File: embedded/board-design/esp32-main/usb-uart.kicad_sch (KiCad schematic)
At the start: 16 parts, among them J2 0473460001, U3 FT231XS

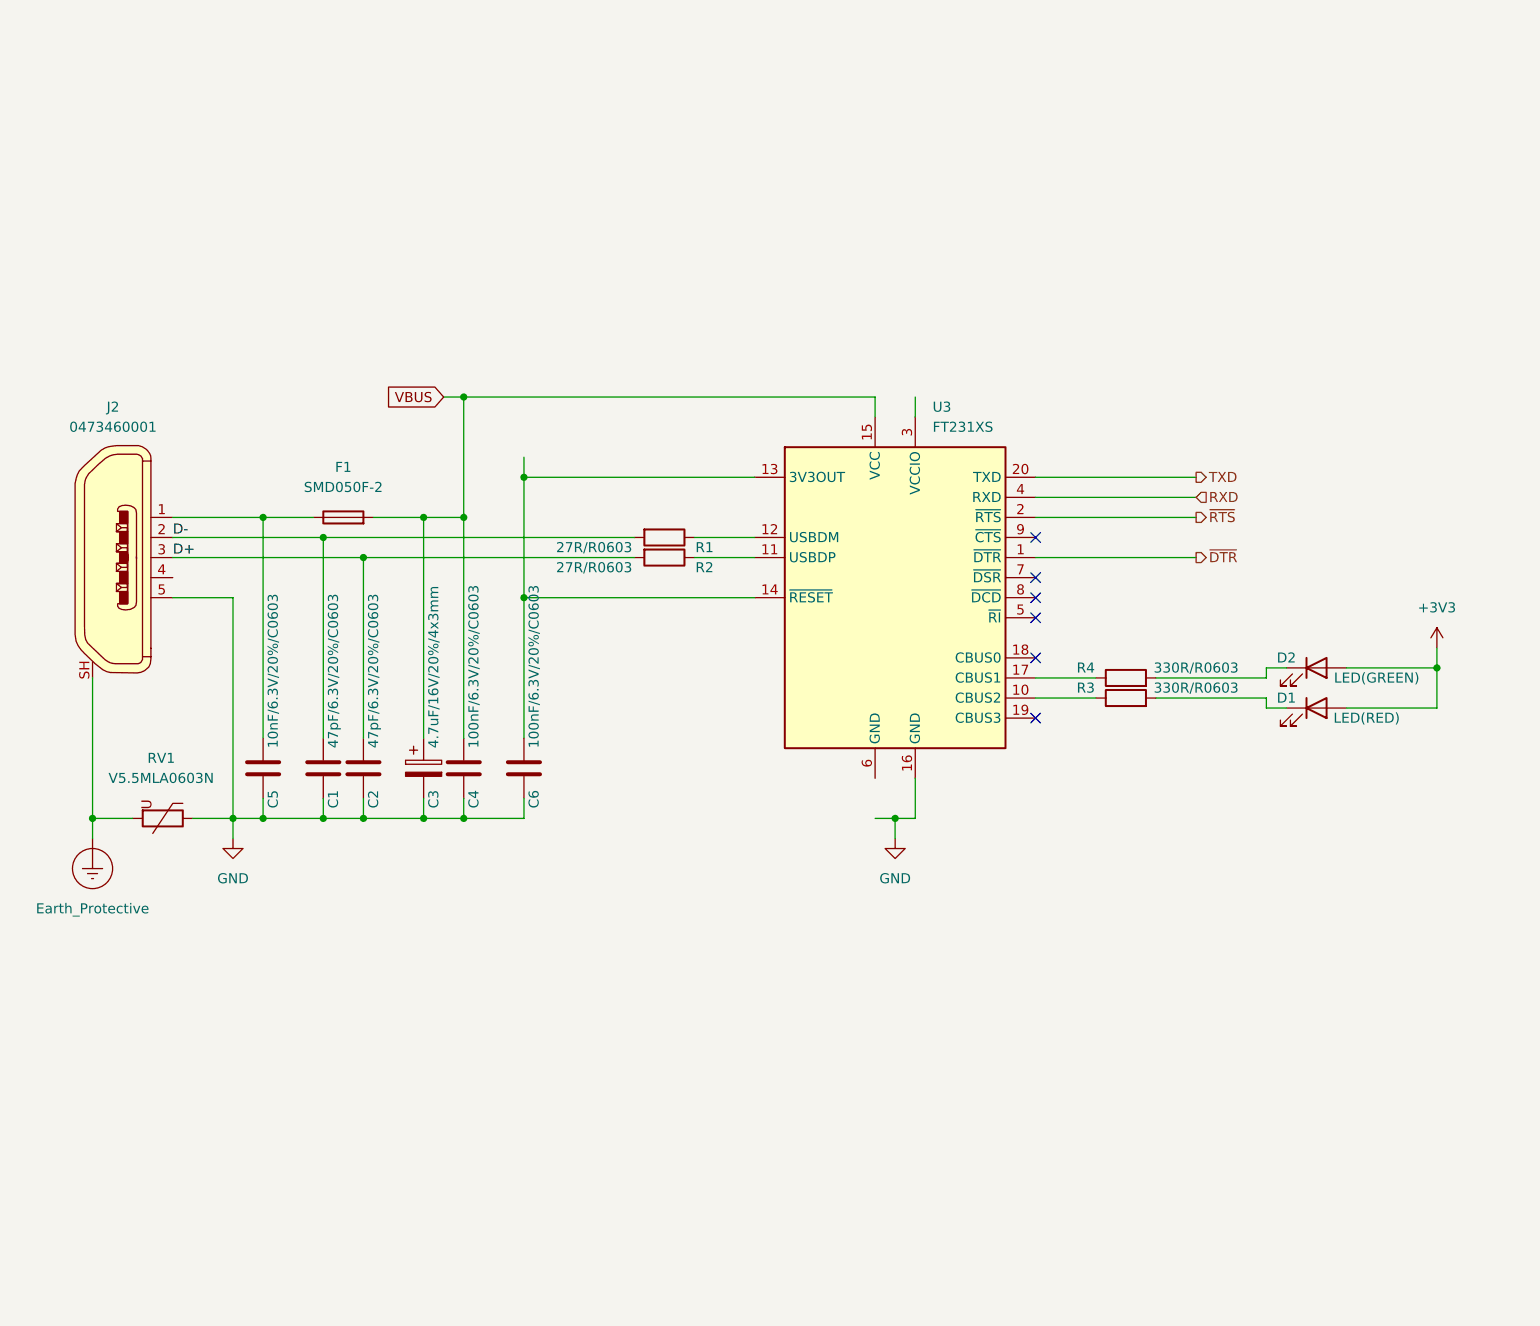
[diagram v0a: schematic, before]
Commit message: [bike-embedded-app]
Finished first schematic draft.

Signed-off-by: Nicolae-Andrei Vasile <vasilenicolaeandrei@gmail.com>
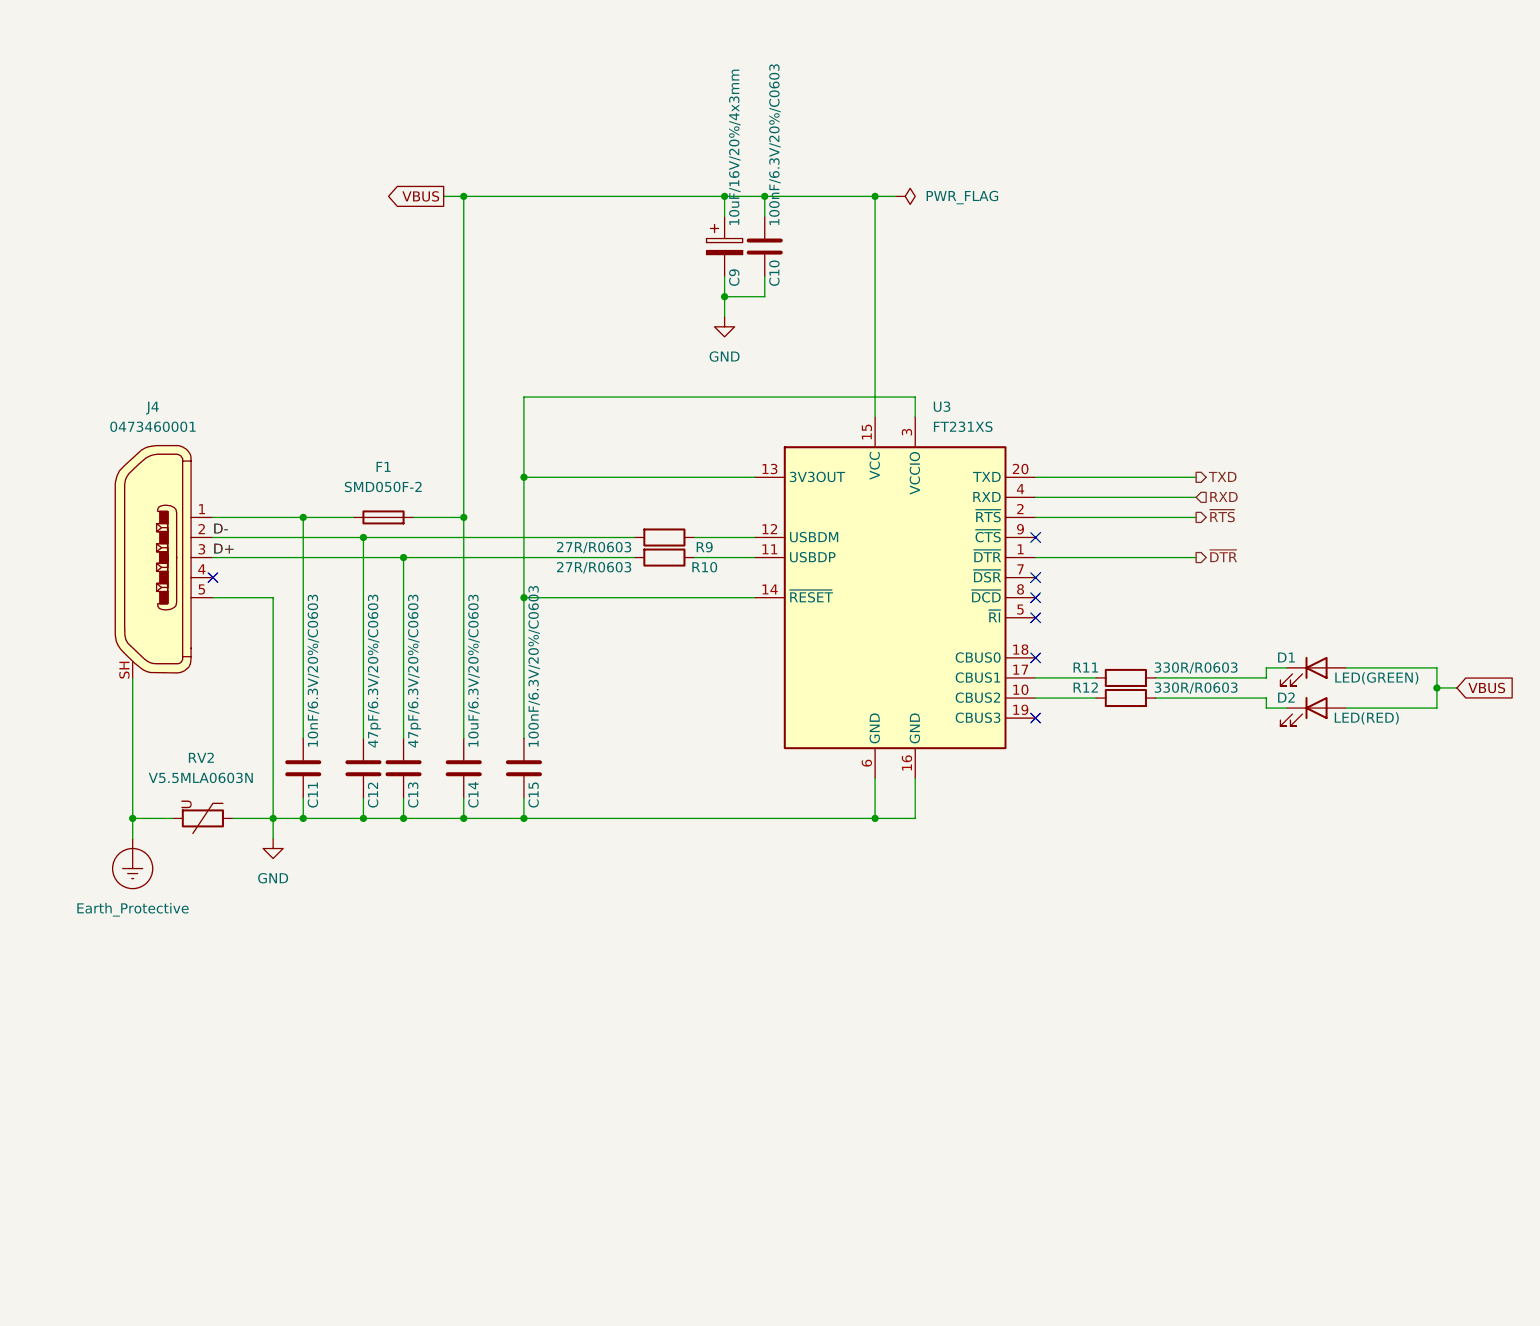
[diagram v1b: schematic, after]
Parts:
- added C14: 10uF/6.3V/20%/C0603, Capacitor_SMD:C_0603_1608Metric_Pad1.08x0.95mm_HandSolder, symbol Device:C
- C9: renamed from C3; value 4.7uF/16V/20%/4x3mm -> 10uF/16V/20%/4x3mm
- RV2: renamed from RV1; footprint (none) -> Resistor_SMD:R_0603_1608Metric_Pad0.98x0.95mm_HandSolder
- renumbered C4 to C10, C5 to C11, C1 to C12, C2 to C13, C6 to C15, D2 to D1, D1 to D2, J2 to J4, R2 to R10, R4 to R11, R3 to R12, R1 to R9
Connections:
- net +3V3 is gone; now on net VBUS: D1.2 (A), D2.2 (A)
- net GND: now also U3.6 (GND), C14.2
- net VBUS: now also C14.1
- net at C15.1, U3.13 (3V3OUT), U3.14 (~{RESET}): now also U3.3 (VCCIO)
- no-connect marks 6 -> 7
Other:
- moved on the sheet: C10, C11, C12, C13, C9, F1, J4, RV2

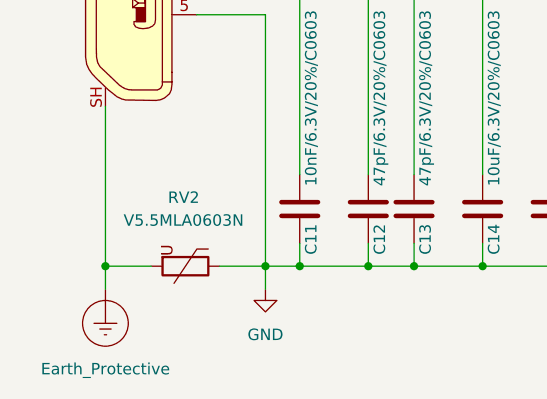
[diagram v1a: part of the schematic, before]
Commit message: [bike-embedded-app]
Finished first draft of the embedded hardware app. PCB design
constraints follow PCBWay recommendations.

Signed-off-by: Nicolae-Andrei Vasile <vasilenicolaeandrei@gmail.com>
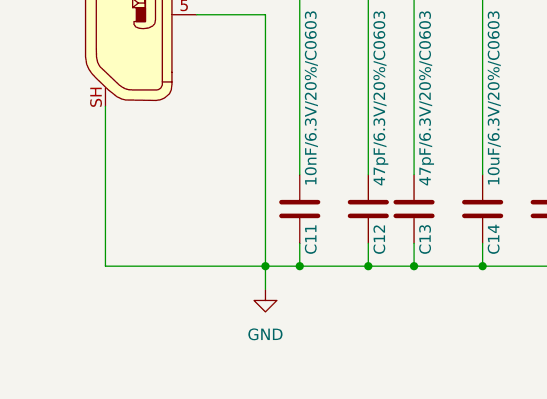
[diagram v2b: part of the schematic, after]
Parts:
- removed RV2: V5.5MLA0603N, Resistor_SMD:R_0603_1608Metric_Pad0.98x0.95mm_HandSolder, symbol Device:Varistor
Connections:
- net Earth_Protective is gone; now on net GND: J4.SH
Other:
- title: (none) -> ESP32 embedded application

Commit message: [bike-embedded-app]
Signed-off-by: Nicolae-Andrei Vasile <vasilenicolaeandrei@gmail.com>
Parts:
- added J5: Conn_01x02_Socket, Connector_PinHeader_1.27mm:PinHeader_1x02_P1.27mm_Vertical, symbol Connector:Conn_01x02_Socket
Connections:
- net GND: now also J5.2 (Pin_2)
- net VBUS: now also J5.1 (Pin_1)
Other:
- note added: "VBUS - 5V MAX!"
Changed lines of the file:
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@@
 	(wire
 		(pts
+			(xy 127 176.53) (xy 139.7 176.53)
+		)
+		(stroke
+			(width 0)
+			(type default)
+		)
+	)
+	(wire
+		(pts
 			(xy 148.59 60.96) (xy 148.59 63.5)
 		)
@@
 	(wire
 		(pts
+			(xy 127 179.07) (xy 127 181.61)
+		)
+		(stroke
+			(width 0)
+			(type default)
+		)
+	)
+	(wire
+		(pts
 			(xy 118.11 86.36) (xy 147.32 86.36)
 		)
@@
 		)
 	)
+	(polyline
+		(pts
+			(xy 114.3 191.77) (xy 171.45 191.77)
+		)
+		(stroke
+			(width 0)
+			(type default)
+		)
+	)
 	(wire
 		(pts
@@
 		)
 	)
+	(polyline
+		(pts
+			(xy 171.45 166.37) (xy 114.3 166.37)
+		)
+		(stroke
+			(width 0)
+			(type default)
+		)
+	)
 	(wire
 		(pts
@@
 	(wire
 		(pts
+			(xy 139.7 179.07) (xy 127 179.07)
+		)
+		(stroke
+			(width 0)
+			(type default)
+		)
+	)
+	(wire
+		(pts
 			(xy 68.58 111.76) (xy 68.58 129.54)
 		)
@@
 		)
 	)
+	(polyline
+		(pts
+			(xy 171.45 191.77) (xy 171.45 166.37)
+		)
+		(stroke
+			(width 0)
+			(type default)
+		)
+	)
 	(wire
 		(pts
@@
 		)
 	)
+	(polyline
+		(pts
+			(xy 114.3 166.37) (xy 114.3 191.77)
+		)
+		(stroke
+			(width 0)
+			(type default)
+		)
+	)
 	(wire
 		(pts
@@
 		)
 	)
+	(text "VBUS - 5V MAX!"
+		(exclude_from_sim no)
+		(at 124.46 168.91 0)
+		(effects
+			(font
+				(size 1.27 1.27)
+			)
+		)
+	)
 	(label "D+"
 		(at 78.74 96.52 0)
@@
 	)
 	(global_label "VBUS"
+		(shape output)
+		(at 127 176.53 180)
+		(fields_autoplaced yes)
+		(effects
+			(font
+				(size 1.27 1.27)
+			)
+			(justify right)
+		)
+		(property "Intersheetrefs" "${INTERSHEET_REFS}"
+			(at 119.1162 176.53 0)
+			(effects
+				(font
+					(size 1.27 1.27)
+				)
+				(justify right)
+				(hide yes)
+			)
+		)
+	)
+	(global_label "VBUS"
 		(shape input)
 		(at 236.22 113.03 0)
@@
 	)
 	(symbol
+		(lib_id "Connector:Conn_01x02_Socket")
+		(at 144.78 176.53 0)
+		(unit 1)
+		(exclude_from_sim no)
+		(in_bom yes)
+		(on_board yes)
+		(dnp no)
+		(fields_autoplaced yes)
+		(property "Reference" "J5"
+			(at 146.05 176.5299 0)
+			(effects
+				(font
+					(size 1.27 1.27)
+				)
+				(justify left)
+			)
+		)
+		(property "Value" "Conn_01x02_Socket"
+			(at 146.05 179.0699 0)
+			(effects
+				(font
+					(size 1.27 1.27)
+				)
+				(justify left)
+			)
+		)
+		(property "Footprint" "Connector_PinHeader_1.27mm:PinHeader_1x02_P1.27mm_Vertical"
+			(at 144.78 176.53 0)
+			(effects
+				(font
+					(size 1.27 1.27)
+				)
+				(hide yes)
+			)
+		)
+		(property "Datasheet" "~"
+			(at 144.78 176.53 0)
+			(effects
+				(font
+					(size 1.27 1.27)
+				)
+				(hide yes)
+			)
+		)
+		(property "Description" "Generic connector, single row, 01x02, script generated"
+			(at 144.78 176.53 0)
+			(effects
+				(font
+					(size 1.27 1.27)
+				)
+				(hide yes)
+			)
+		)
+		(pin "1"
+		)
+		(pin "2"
+		)
+		(instances
+			(project "esp32-main"
+				(path "/6d02e045-d1b3-4320-a4f8-f5e2c734acd4/7d21a99c-c3fd-4678-bc5b-fcb8ce659019"
+					(reference "J5")
+					(unit 1)
+				)
+			)
+		)
+	)
+	(symbol
 		(lib_id "Device:R")
 		(at 194.31 114.3 90)
@@
 					(unit 1)
 				)
+			)
+		)
+	)
+	(symbol
+		(lib_id "power:GND")
+		(at 127 181.61 0)
+		(unit 1)
+		(exclude_from_sim no)
+		(in_bom yes)
+		(on_board yes)
+		(dnp no)
+		(fields_autoplaced yes)
+		(property "Reference" "#PWR015"
+			(at 127 187.96 0)
+			(effects
+				(font
+					(size 1.27 1.27)
+				)
+				(hide yes)
+			)
+		)
+		(property "Value" "GND"
+			(at 127 186.69 0)
+			(effects
+				(font
+					(size 1.27 1.27)
+				)
+			)
+		)
+		(property "Footprint" ""
+			(at 127 181.61 0)
+			(effects
+				(font
+					(size 1.27 1.27)
+				)
+				(hide yes)
+			)
+		)
+		(property "Datasheet" ""
+			(at 127 181.61 0)
+			(effects
+				(font
+					(size 1.27 1.27)
+				)
+				(hide yes)
+			)
+		)
+		(property "Description" "Power symbol creates a global label with name \"GND\" , ground"
+			(at 127 181.61 0)
+			(effects
+				(font
+					(size 1.27 1.27)
+				)
+				(hide yes)
+			)
+		)
+		(pin "1"
+		)
+		(instances
+			(project "esp32-main"
+				(path "/6d02e045-d1b3-4320-a4f8-f5e2c734acd4/7d21a99c-c3fd-4678-bc5b-fcb8ce659019"
+					(reference "#PWR015")
+					(unit 1)
+				)
